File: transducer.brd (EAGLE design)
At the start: 33 x 33 mm, 12 parts, among them U1 ADS1014IDGST

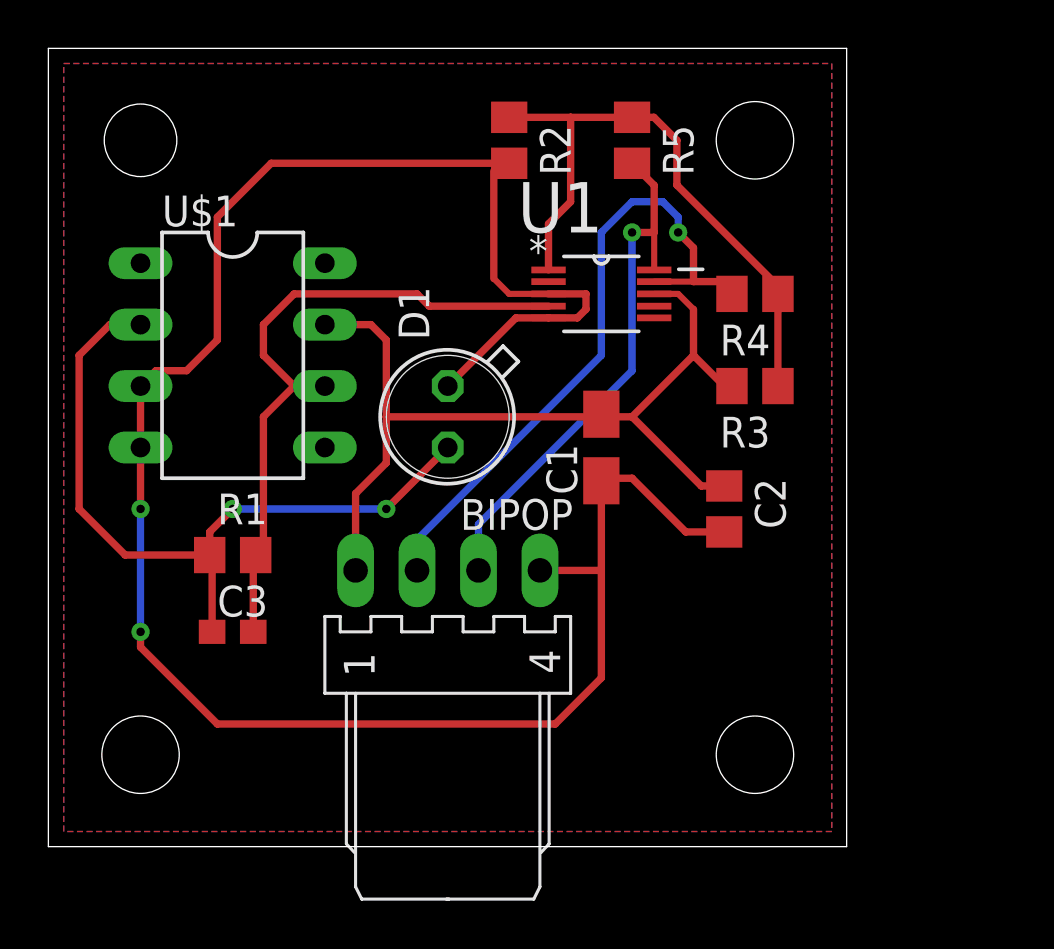
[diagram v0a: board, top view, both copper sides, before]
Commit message: UV transducer board redesigned according to SGlux tips
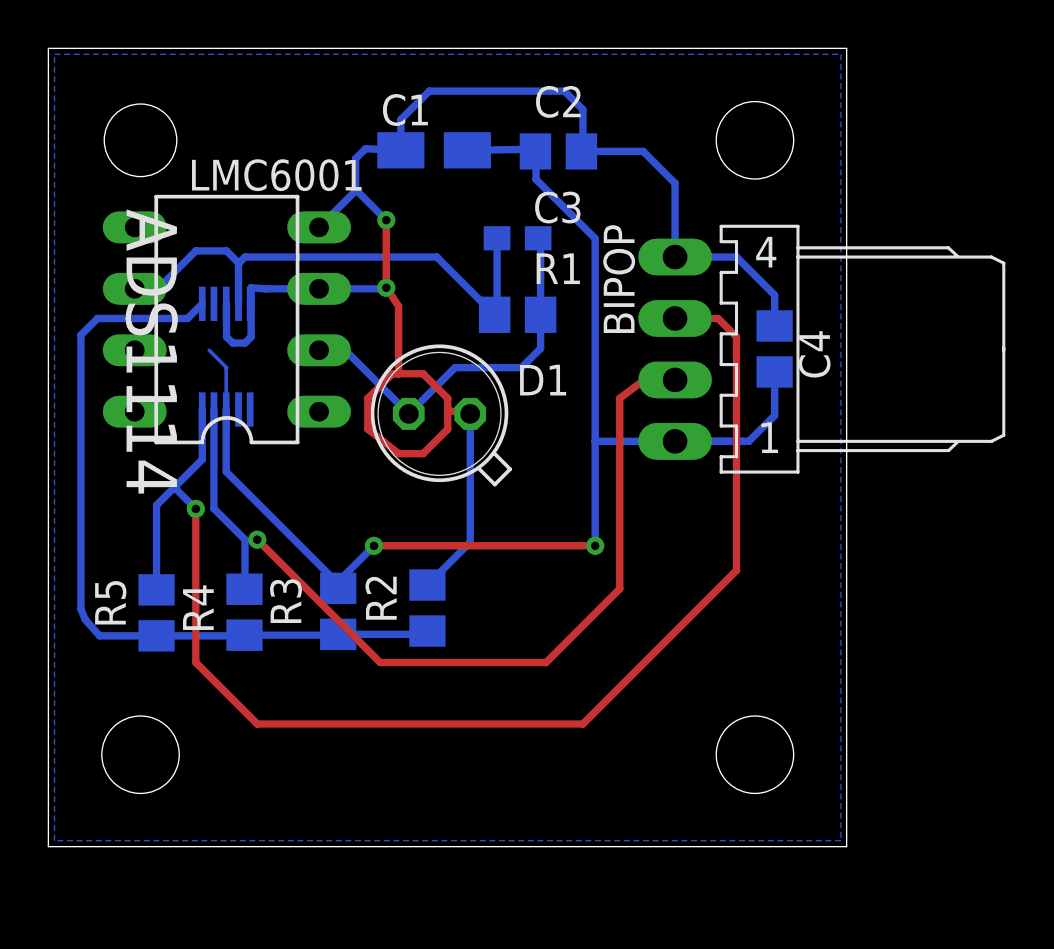
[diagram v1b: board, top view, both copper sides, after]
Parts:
- removed U$1: LMC6001, customy:DIL08
- removed U1: ADS1014IDGST, Texas Instruments_By_element14_Batch_1:SOP50P490X110-10N
- added ADS1114: ADS1014IDGST, Texas Instruments_By_element14_Batch_1:SOP50P490X110-10N
- added C4: 4.7µ, rcl:C0805
- added LMC6001: LMC6001, customy:DIL08
- moved R5 27.7 mm to (4.47, 56.7), flipped to the bottom, turned to 90 degrees
- moved R4 24.9 mm to (8.11, 56.7), flipped to the bottom, turned to 90 degrees
- moved C3 20.1 mm to (19.4, 72.2), flipped to the bottom
- moved R2 19.6 mm to (15.7, 56.9), flipped to the bottom, turned to 90 degrees
- moved R3 19.6 mm to (12.0, 56.7), flipped to the bottom, turned to 90 degrees
- moved C2 16.3 mm to (21.1, 75.7), flipped to the bottom, turned to 180 degrees
- moved R1 15.4 mm to (19.4, 69.0), flipped to the bottom
- moved C1 14.1 mm to (15.9, 75.8), flipped to the bottom, turned to 180 degrees
- moved BIPOP 13.1 mm to (25.9, 67.6), turned to 270 degrees
- moved D1 0.36 mm to (16.2, 64.9), turned to 0 degrees
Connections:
- removed net 3.3V: BIPOP.1, C1.+, C2.1, R3.2, U$1.7, U1.8
- removed net N$5: C3.1, D1.C, R1.1, U$1.2
- new net 5V: ADS1114.8, BIPOP.1, C1.+, C2.1, C4.1, LMC6001.7, R3.2
- new net CATH: C3.1, D1.C, LMC6001.2, R1.1
- net ADR: now also ADS1114.1; no longer U1.1
- net GND: now also ADS1114.3, ADS1114.5, C4.2, LMC6001.3, LMC6001.4; no longer U$1.3, U$1.4, U1.3, U1.5
- net N$8: now also ADS1114.2; no longer U1.2
- net SCL: now also ADS1114.10; no longer U1.10
- net SDA: now also ADS1114.9; no longer U1.9
- net U_OUT: now also ADS1114.4, LMC6001.6; no longer U$1.6, U1.4
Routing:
- net 5V: track 0.00 -> 55.9 mm, vias 0 -> 2
- net 3.3V: track 37.6 -> 0.00 mm
- net SCL: track 22.3 -> 54.4 mm
- net N$5: track 31.0 -> 0.00 mm, vias 2 -> 0
- net GND: track 86.9 -> 68.9 mm
- net CATH: track 0.00 -> 16.0 mm
- net SDA: track 27.4 -> 37.2 mm
- net U_OUT: track 28.3 -> 21.7 mm
- net ADR: track 25.9 -> 31.9 mm
- removed copper zone on layer 1, net GND

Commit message: BIPOP board redesigned, new versions of transducers added.
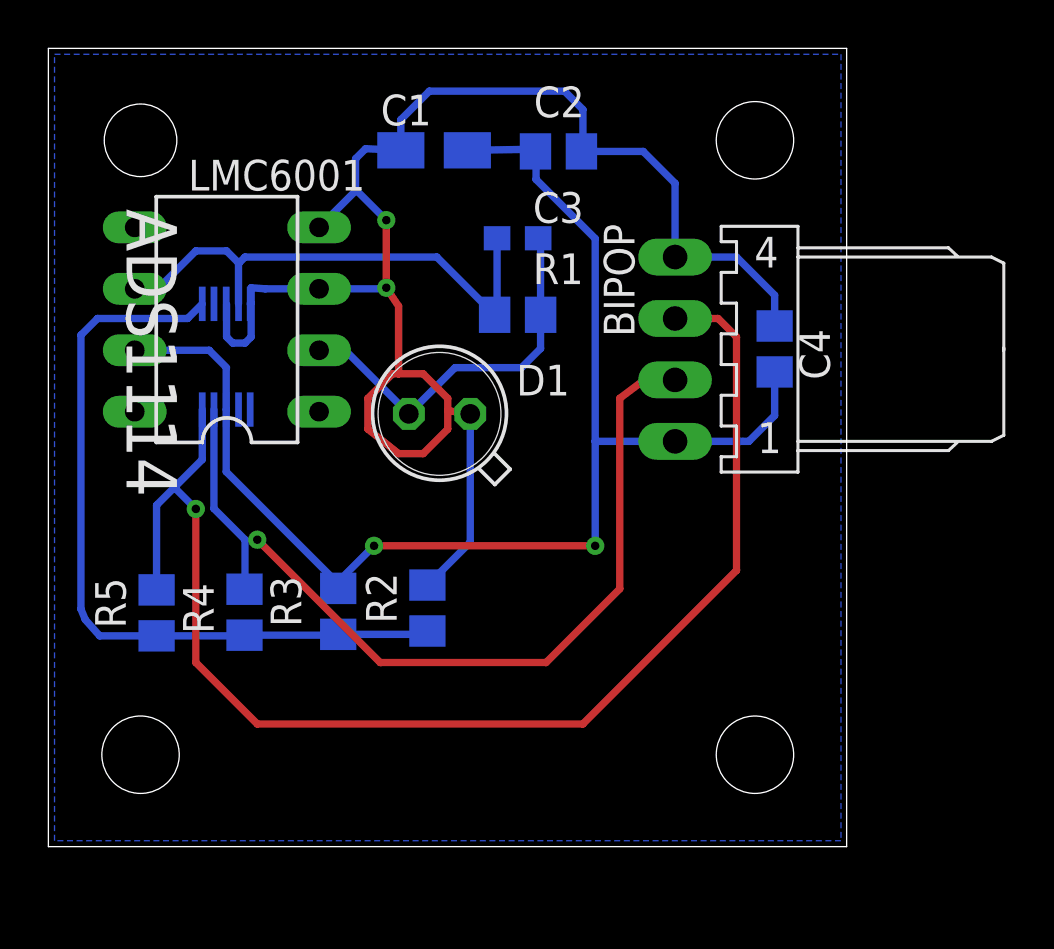
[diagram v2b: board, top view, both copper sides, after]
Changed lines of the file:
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@@
 <wire x1="20.16" y1="74.582" x2="22.606" y2="72.136" width="0.3048" layer="16"/>
 <contactref element="ADS1114" pad="8"/>
-<wire x1="6.648" y1="67.52" x2="7.366" y2="66.802" width="0.1524" layer="16"/>
+<wire x1="7.366" y1="66.802" x2="6.648" y2="67.52" width="0.3048" layer="16"/>
 <wire x1="7.366" y1="66.802" x2="7.352" y2="66.788" width="0.1524" layer="16"/>
-<wire x1="7.352" y1="66.788" x2="7.352" y2="65.0696" width="0.1524" layer="16"/>
+<wire x1="7.352" y1="66.788" x2="7.352" y2="65.0696" width="0.3048" layer="16"/>
 <wire x1="7.352" y1="65.0696" x2="7.352" y2="62.498" width="0.3048" layer="16"/>
 <wire x1="7.352" y1="62.498" x2="11.98" y2="57.87" width="0.3048" layer="16"/>
-<wire x1="28.702" y1="63.754" x2="22.606" y2="63.754" width="0.3048" layer="16"/>
-<wire x1="6.648" y1="67.52" x2="3.57" y2="67.52" width="0" layer="19" extent="16-16"/>
+<wire x1="25.908" y1="63.754" x2="22.606" y2="63.754" width="0.3048" layer="16"/>
+<wire x1="6.648" y1="67.52" x2="3.57" y2="67.52" width="0.3048" layer="16"/>
+<wire x1="11.98" y1="57.87" x2="11.98" y2="57.676" width="0" layer="19" extent="16-16"/>
 <wire x1="11.98" y1="57.954" x2="11.98" y2="57.87" width="0" layer="19" extent="16-16"/>
-<wire x1="11.98" y1="57.676" x2="11.98" y2="57.87" width="0" layer="19" extent="16-16"/>
 </signal>
 </signals>
